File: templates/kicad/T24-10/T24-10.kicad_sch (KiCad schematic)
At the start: 10 parts

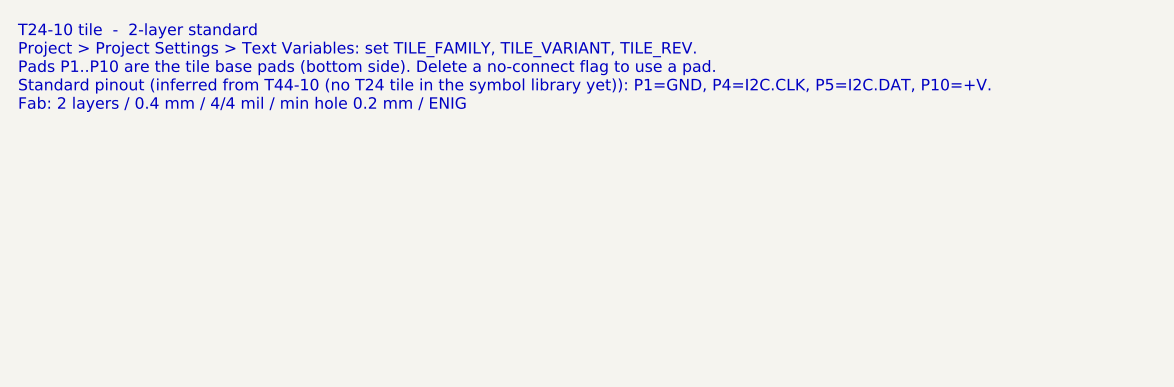
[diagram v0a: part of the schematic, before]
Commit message: Re-tier on measured prices: 4L on 0.2 mm drill, add 4L-fine
4L keeps the 0.2 mm drill so it lands in PCBWay's $162 standard bucket
rather than the $419 one; 3/3 mil and 0.15 mm drills move to a new 4L-fine
tier on the advanced form. Quotes name the calculator to use. set_tier.py
gains --package for projects that predate the templates and --ignore-locks
for stale lock files.

Co-Authored-By: Claude Fable 5.1 <noreply@anthropic.com>
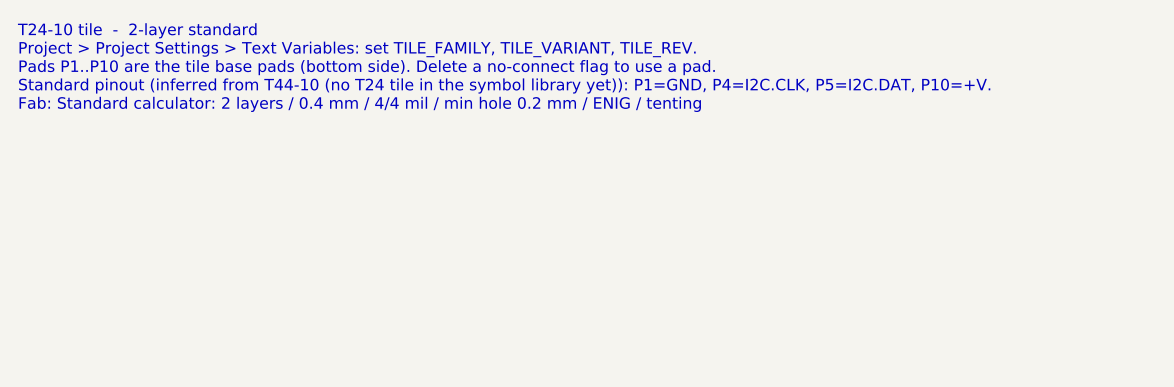
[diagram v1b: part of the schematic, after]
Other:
- note added: "T24-10 tile - 2-layer standard Project > Project Settings > Text Variables: set TILE_FAMILY, TILE_VARIANT, TILE_REV. Pads P1..P10 are the tile base pads (bottom side). Delete a no-connect flag to use a pad. Standard pinout (inferred from T44-10 (no T24 tile in the symbol library yet)): P1=GND, P4=I2C.CLK, P5=I2C.DAT, P10=+V. Fab: Standard calculator: 2 layers / 0.4 mm / 4/4 mil / min hole 0.2 mm 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"
- note removed: "T24-10 tile - 2-layer standard Project > Project Settings > Text Variables: set TILE_FAMILY, TILE_VARIANT, TILE_REV. Pads P1..P10 are the tile base pads (bottom side). Delete a no-connect flag to use a pad. Standard pinout (inferred from T44-10 (no T24 tile in the symbol library yet)): P1=GND, P4=I2C.CLK, P5=I2C.DAT, P10=+V. Fab: 2 layers / 0.4 mm / 4/4 mil / min hole 0.2 mm / ENIG"
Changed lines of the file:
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@@
 		(comment 2 "${FAB_QUOTE}")
 	)
-	(text "T24-10 tile  -  2-layer standard\nProject > Project Settings > Text Variables: set TILE_FAMILY, TILE_VARIANT, TILE_REV.\nPads P1..P10 are the tile base pads (bottom side). Delete a no-connect flag to use a pad.\nStandard pinout (inferred from T44-10 (no T24 tile in the symbol library yet)): P1=GND, P4=I2C.CLK, P5=I2C.DAT, P10=+V.\nFab: 2 layers / 0.4 mm / 4/4 mil / min hole 0.2 mm / ENIG"
+	(text "T24-10 tile  -  2-layer standard\nProject > Project Settings > Text Variables: set TILE_FAMILY, TILE_VARIANT, TILE_REV.\nPads P1..P10 are the tile base pads (bottom side). Delete a no-connect flag to use a pad.\nStandard pinout (inferred from T44-10 (no T24 tile in the symbol library yet)): P1=GND, P4=I2C.CLK, P5=I2C.DAT, P10=+V.\nFab: Standard calculator: 2 layers / 0.4 mm / 4/4 mil / min hole 0.2 mm / ENIG / tenting"
 		(exclude_from_sim no)
 		(at 25.4 25.4 0)
